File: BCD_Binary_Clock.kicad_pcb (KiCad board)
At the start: 2 copper layers, 134.5 x 47 mm, 52 parts, among them J1 PinSocket_1x06_P2.54mm_Vertic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, SW1 HRS BUTTON, SW2 MIN BUTTON, U1 74HC595, U2 74HC595, U3 74HC595

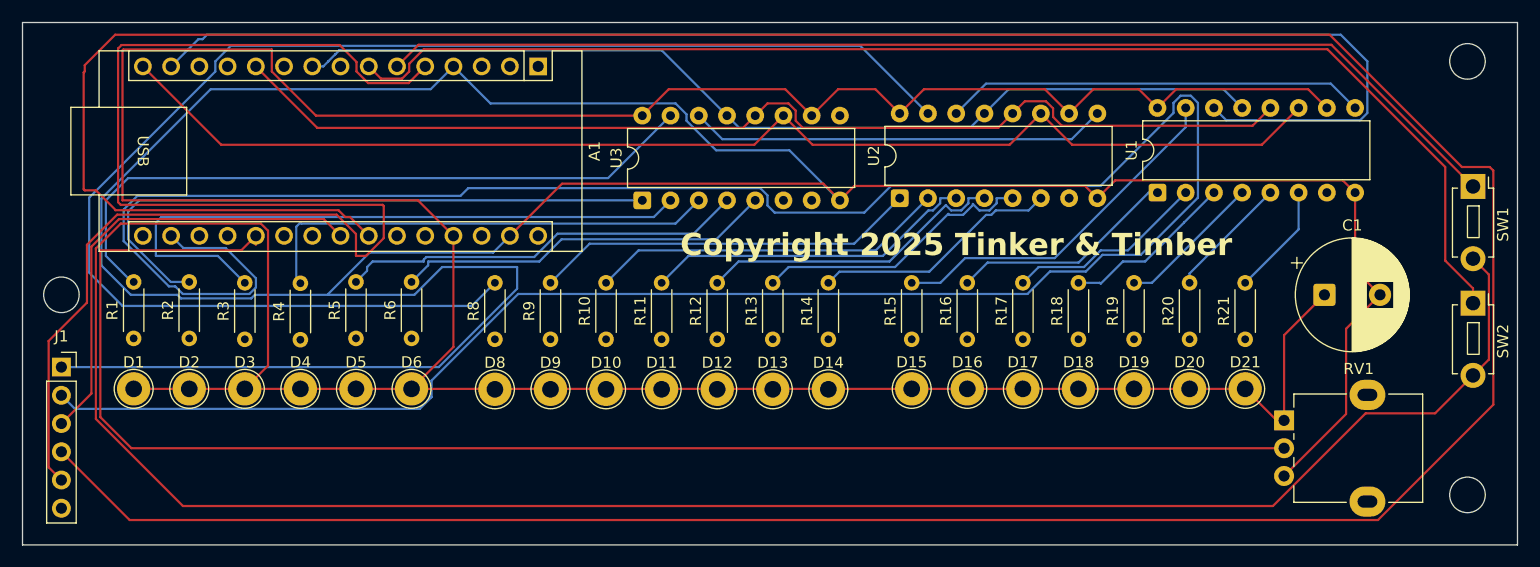
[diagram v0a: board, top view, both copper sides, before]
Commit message: Fixed SW1 & SW2 going to VCC - now pulling to GNC
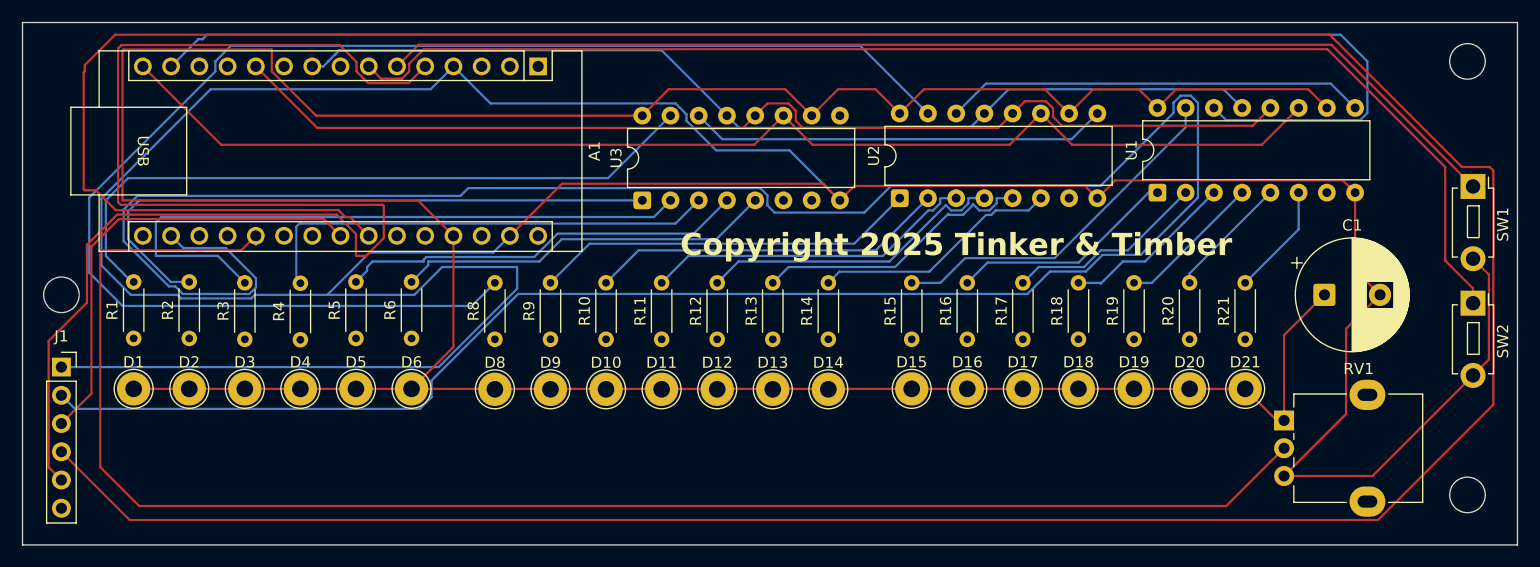
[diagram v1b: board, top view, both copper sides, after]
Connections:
- SW1 pad 2: VCC -> GND
- SW2 pad 2: VCC -> GND
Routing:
- net VCC: track 488.9 -> 298.1 mm
- net GND: track 297.7 -> 330.1 mm
- net Net-(A1-A1): track 138.0 -> 145.0 mm
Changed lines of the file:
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@@
 			(layers "*.Cu" "*.Mask")
 			(remove_unused_layers no)
-			(net 4 "VCC")
+			(net 1 "GND")
 			(pinfunction "2")
 			(pintype "passive")
@@
 			(layers "*.Cu" "*.Mask")
 			(remove_unused_layers no)
-			(net 4 "VCC")
+			(net 1 "GND")
 			(pinfunction "2")
 			(pintype "passive")
@@
 	)
 	(segment
+		(start 181.926 73.176)
+		(end 181.926 80.824)
+		(width 0.2)
+		(layer "F.Cu")
+		(net 1)
+	)
+	(segment
+		(start 181.926 80.824)
+		(end 180.5 82.25)
+		(width 0.2)
+		(layer "F.Cu")
+		(net 1)
+	)
+	(segment
 		(start 169.89 72.757677)
 		(end 172.132323 75)
@@
 	)
 	(segment
+		(start 177.125 85.625)
+		(end 171.45 91.3)
+		(width 0.2)
+		(layer "F.Cu")
+		(net 1)
+	)
+	(segment
 		(start 122.04 65)
 		(end 98.54 65)
@@
 	)
 	(segment
+		(start 180.5 82.25)
+		(end 177.125 85.625)
+		(width 0.2)
+		(layer "F.Cu")
+		(net 1)
+	)
+	(segment
 		(start 124.836 65.204)
 		(end 123.54 66.5)
@@
 	)
 	(segment
+		(start 171.45 91.3)
+		(end 163.5 91.3)
+		(width 0.2)
+		(layer "F.Cu")
+		(net 1)
+	)
+	(segment
 		(start 168.789 64.704)
 		(end 148.301 64.704)
@@
 	)
 	(segment
+		(start 180.5 71.75)
+		(end 181.926 73.176)
+		(width 0.2)
+		(layer "F.Cu")
+		(net 1)
+	)
+	(segment
 		(start 145.599 65.204)
 		(end 124.836 65.204)
@@
 	)
 	(segment
-		(start 181.926 73.176)
-		(end 181.926 80.824)
-		(width 0.2)
-		(layer "F.Cu")
-		(net 4)
-	)
-	(segment
 		(start 85.58 66.5)
 		(end 88.77 69.69)
@@
 	)
 	(segment
-		(start 181.926 80.824)
-		(end 180.5 82.25)
-		(width 0.2)
-		(layer "F.Cu")
-		(net 4)
-	)
-	(segment
 		(start 59.071 52.929)
 		(end 59 53)
@@
 	)
 	(segment
-		(start 58.8439 68.589)
-		(end 71.44605 68.589)
-		(width 0.2)
-		(layer "F.Cu")
-		(net 4)
-	)
-	(segment
-		(start 180.5 82.25)
-		(end 177.089 85.661)
-		(width 0.2)
-		(layer "F.Cu")
-		(net 4)
-	)
-	(segment
 		(start 152.11 58.185)
 		(end 153.795 56.5)
@@
 	)
 	(segment
-		(start 170.837471 85.661)
-		(end 162.498471 94)
-		(width 0.2)
-		(layer "F.Cu")
-		(net 4)
-	)
-	(segment
-		(start 56.599 86.1661)
-		(end 56.599 70.8339)
-		(width 0.2)
-		(layer "F.Cu")
-		(net 4)
-	)
-	(segment
 		(start 163.5 86.3)
 		(end 162.84 86.3)
@@
 	)
 	(segment
-		(start 177.089 85.661)
-		(end 170.837471 85.661)
-		(width 0.2)
-		(layer "F.Cu")
-		(net 4)
-	)
-	(segment
 		(start 145 83.46)
 		(end 140 83.46)
@@
 	)
 	(segment
-		(start 72.091 69.23395)
-		(end 72.091 81.369)
-		(width 0.2)
-		(layer "F.Cu")
-		(net 4)
-	)
-	(segment
-		(start 180.5 71.75)
-		(end 181.926 73.176)
-		(width 0.2)
-		(layer "F.Cu")
-		(net 4)
-	)
-	(segment
-		(start 64.4329 94)
-		(end 56.599 86.1661)
-		(width 0.2)
-		(layer "F.Cu")
-		(net 4)
-	)
-	(segment
-		(start 56.599 70.8339)
-		(end 58.8439 68.589)
-		(width 0.2)
-		(layer "F.Cu")
-		(net 4)
-	)
-	(segment
 		(start 121 58.88)
 		(end 118.62 56.5)
@@
 	)
 	(segment
-		(start 72.091 81.369)
-		(end 70 83.46)
-		(width 0.2)
-		(layer "F.Cu")
-		(net 4)
-	)
-	(segment
-		(start 162.498471 94)
-		(end 64.4329 94)
-		(width 0.2)
-		(layer "F.Cu")
-		(net 4)
-	)
-	(segment
-		(start 71.44605 68.589)
-		(end 72.091 69.23395)
-		(width 0.2)
-		(layer "F.Cu")
-		(net 4)
-	)
-	(segment
 		(start 105.76 58.88)
 		(end 76.40295 58.88)
@@
 	)
 	(segment
-		(start 57 86)
-		(end 57 71)
+		(start 70.99 70.51)
+		(end 70.99 69.69)
 		(width 0.2)
 		(layer "F.Cu")
@@
 	)
 	(segment
-		(start 70.99 70.51)
-		(end 70.99 69.69)
+		(start 60.5 94)
+		(end 57 90.5)
 		(width 0.2)
 		(layer "F.Cu")
@@
 	)
 	(segment
-		(start 163.5 88.8)
-		(end 59.8 88.8)
+		(start 57 90.5)
+		(end 57 71)
 		(width 0.2)
 		(layer "F.Cu")
@@
 	)
 	(segment
-		(start 59.8 88.8)
-		(end 57 86)
+		(start 69.68 71)
+		(end 70.99 69.69)
+		(width 0.2)
+		(layer "F.Cu")
+		(net 17)
+	)
+	(segment
+		(start 163.5 88.8)
+		(end 158.3 94)
 		(width 0.2)
 		(layer "F.Cu")
@@
 	)
 	(segment
-		(start 69.68 71)
-		(end 70.99 69.69)
+		(start 158.3 94)
+		(end 60.5 94)
 		(width 0.2)
 		(layer "F.Cu")
@@
 	)
 	(group ""
-		(members "061e2465-0b60-409d-b607-212d9cda1826" "08382b3b-32c0-440d-980e-f0db1f2525f1"
-			"0f255973-0ae2-451e-92df-407ea259a171" "2fb50520-0541-4aaa-9277-2f95e8549fbb"
-			"3d418252-8ee7-419c-9449-b1c924ae5d31" "4eca6b13-91cc-4586-a736-f6da2cfa0081"
-			"55532816-2291-4a33-89af-0ee056795d50" "575143db-9111-4a26-beb1-8e893be5ccc2"
-			"5853b4e1-47d8-486f-bad8-f48429d39485" "7151adc1-d706-4578-be48-64d0a96f44d5"
-			"8621e9c3-d7fe-465c-9f4f-6030afe7fe3a" "949558e6-20d1-45e3-8541-03eb588715a7"
-			"aa48f24d-52b3-463e-9b36-42d8c85e1b7e" "e44d3a7f-3a4f-4dea-87a8-97a6a707c9b4"
-		)
-	)
-	(group ""
 		(members "26a8619e-7f2e-4b82-ab44-75195a4c1eeb" "3084b45b-3dd9-4eab-abf0-9c2a17bc93ef"
 			"36ac6f10-21de-40a4-a620-01ae79d84c3b" "3808c8eb-2177-4b69-9091-5fe499b67ad0"
@@
 		)
 	)
+	(group ""
+		(members "061e2465-0b60-409d-b607-212d9cda1826" "08382b3b-32c0-440d-980e-f0db1f2525f1"
+			"0f255973-0ae2-451e-92df-407ea259a171" "2fb50520-0541-4aaa-9277-2f95e8549fbb"
+			"3d418252-8ee7-419c-9449-b1c924ae5d31" "4eca6b13-91cc-4586-a736-f6da2cfa0081"
+			"55532816-2291-4a33-89af-0ee056795d50" "575143db-9111-4a26-beb1-8e893be5ccc2"
+			"5853b4e1-47d8-486f-bad8-f48429d39485" "7151adc1-d706-4578-be48-64d0a96f44d5"
+			"8621e9c3-d7fe-465c-9f4f-6030afe7fe3a" "949558e6-20d1-45e3-8541-03eb588715a7"
+			"aa48f24d-52b3-463e-9b36-42d8c85e1b7e" "e44d3a7f-3a4f-4dea-87a8-97a6a707c9b4"
+		)
+	)
